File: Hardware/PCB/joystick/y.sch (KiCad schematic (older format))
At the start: 19 parts, among them J6 AudioJack2, J7 AudioJack2, U2 TL074

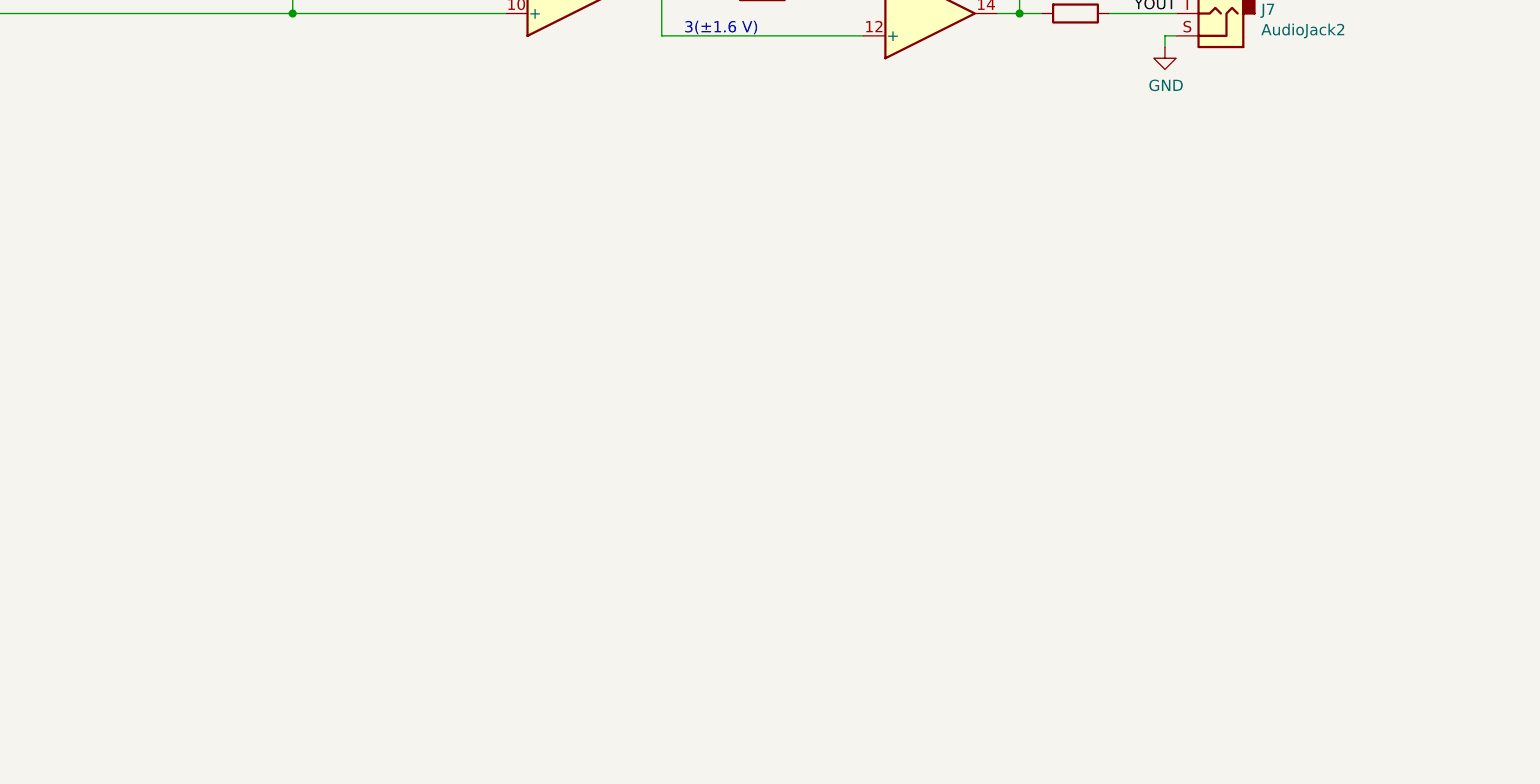
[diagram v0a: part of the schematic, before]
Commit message: Belated .gitignore; switch to panel mounted pots implying board and panel changes
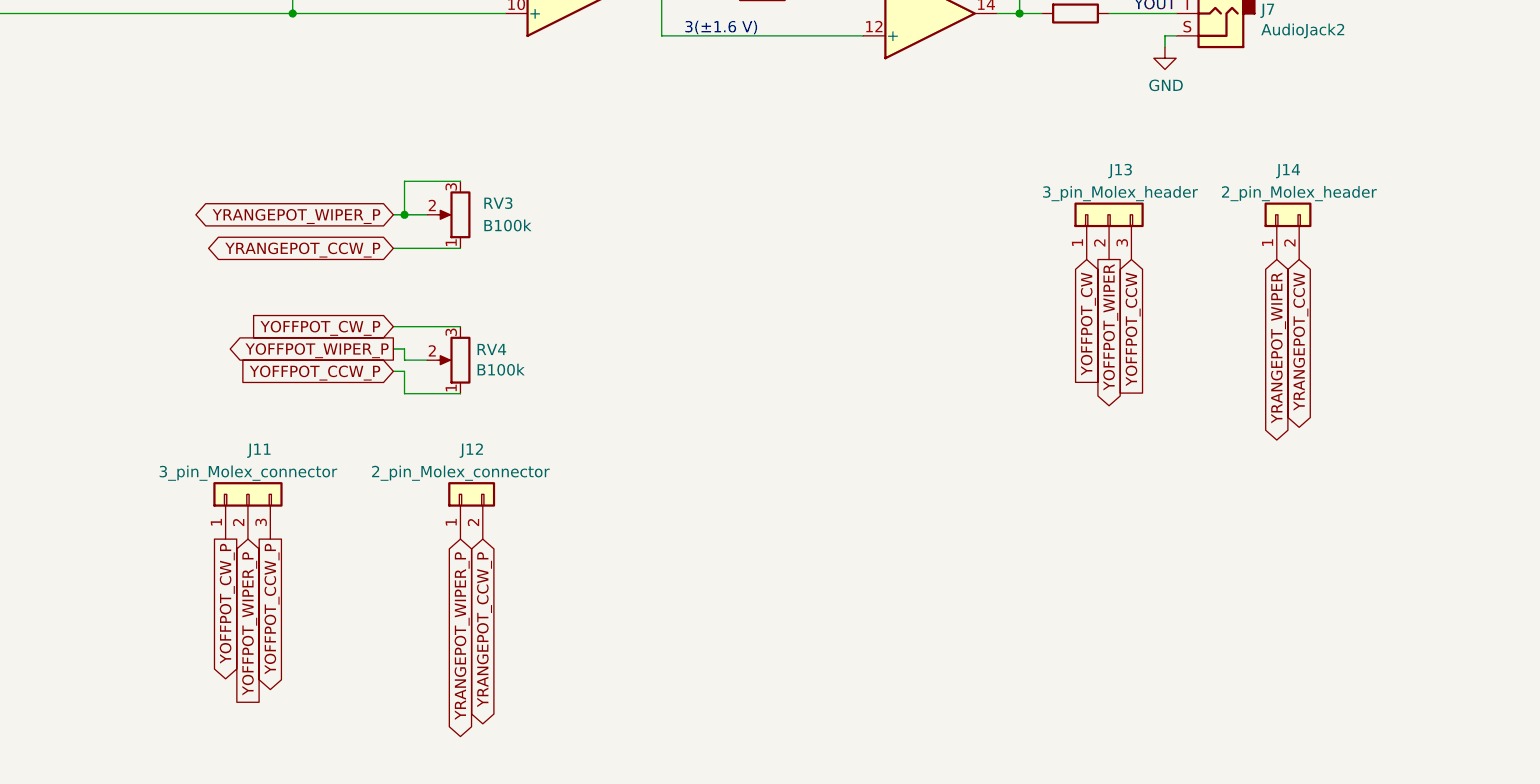
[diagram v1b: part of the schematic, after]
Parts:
- added J11: 3_pin_Molex_connector, symbol ao_symbols:3_pin_Molex_connector
- added J12: 2_pin_Molex_connector, symbol ao_symbols:2_pin_Molex_connector
- added J13: 3_pin_Molex_header, ao_tht:Molex_KK-254_AE-6410-03A_1x03_P2.54mm_Vertical, symbol ao_symbols:3_pin_Molex_header
- added J14: 2_pin_Molex_header, ao_tht:Molex_KK-254_AE-6410-02A_1x02_P2.54mm_Vertical, symbol ao_symbols:2_pin_Molex_header
- added RV3, RV4: B100k, ao_tht:Potentiometer_Alpha_16mm_Single_Vertical, symbol Device:R_POT
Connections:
- net YOFFPOT_CCW: now also J13.3 (Pin_3)
- net YOFFPOT_CW: now also J13.1 (Pin_1)
- net YOFFPOT_WIPER: now also J13.2 (Pin_2)
- net YRANGEPOT_CCW: now also J14.2 (Pin_2)
- net YRANGEPOT_WIPER: now also J14.1 (Pin_1)
- new net YOFFPOT_CCW_P: J11.3 (Pin_3), RV4.1
- new net YOFFPOT_CW_P: J11.1 (Pin_1), RV4.3
- new net YOFFPOT_WIPER_P: J11.2 (Pin_2), RV4.2
- new net YRANGEPOT_CCW_P: J12.2 (Pin_2), RV3.1
- new net YRANGEPOT_WIPER_P: J12.1 (Pin_1), RV3.2, RV3.3
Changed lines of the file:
@@
 $Descr A4 11693 8268
 encoding utf-8
-Sheet 2 3
+Sheet 2 2
 Title ""
 Date ""
@@
 Text GLabel 1850 2250 0    50   Output ~ 0
 YPOT_CCW
+Text GLabel 8600 4550 3    50   Input ~ 0
+YOFFPOT_CW
+Text GLabel 8700 4550 3    50   Output ~ 0
+YOFFPOT_WIPER
+Text GLabel 8800 4550 3    50   Input ~ 0
+YOFFPOT_CCW
+Text GLabel 9550 4550 3    50   BiDi ~ 0
+YRANGEPOT_CCW
+Text GLabel 9450 4550 3    50   BiDi ~ 0
+YRANGEPOT_WIPER
+$Comp
+L ao_symbols:3_pin_Molex_header J?
+U 1 1 617BD456
+P 8700 4350
+AR Path="/617BD456" Ref="J?"  Part="1"
+AR Path="/6157E61D/617BD456" Ref="J13"  Part="1"
+F 0 "J13" V 8900 4350 50  0000 R CNN
+F 1 "3_pin_Molex_header" V 8800 4650 50  0000 R CNN
+F 2 "ao_tht:Molex_KK-254_AE-6410-03A_1x03_P2.54mm_Vertical" H 8700 4350 50  0001 C CNN
+F 3 "" H 8700 4350 50  0001 C CNN
+F 4 "Tayda" H 8700 4350 50  0001 C CNN "Vendor"
+F 5 "A-805" H 8700 4350 50  0001 C CNN "SKU"
+	1    8700 4350
+	0    -1   -1   0
+$EndComp
+$Comp
+L ao_symbols:2_pin_Molex_header J?
+U 1 1 617BD45E
+P 9450 4350
+AR Path="/617BD45E" Ref="J?"  Part="1"
+AR Path="/6157E61D/617BD45E" Ref="J14"  Part="1"
+F 0 "J14" V 9650 4350 50  0000 R CNN
+F 1 "2_pin_Molex_header" V 9550 4600 50  0000 R CNN
+F 2 "ao_tht:Molex_KK-254_AE-6410-02A_1x02_P2.54mm_Vertical" H 9450 4350 50  0001 C CNN
+F 3 "" H 9450 4350 50  0001 C CNN
+F 4 "Tayda" H 9450 4350 50  0001 C CNN "Vendor"
+F 5 "A-804" H 9450 4350 50  0001 C CNN "SKU"
+	1    9450 4350
+	0    -1   -1   0
+$EndComp
+Wire Wire Line
+	5500 5050 5550 5050
+Wire Wire Line
+	5550 5050 5550 5150
+Wire Wire Line
+	5550 5150 5800 5150
+Wire Wire Line
+	5500 4850 5800 4850
+Wire Wire Line
+	5650 5000 5550 5000
+Wire Wire Line
+	5550 5000 5550 4950
+Wire Wire Line
+	5550 4950 5500 4950
+Wire Wire Line
+	5550 4350 5550 4200
+Wire Wire Line
+	5500 4350 5550 4350
+Connection ~ 5550 4350
+Text GLabel 5500 4350 0    50   BiDi ~ 0
+YRANGEPOT_WIPER_P
+Text GLabel 5500 4500 0    50   BiDi ~ 0
+YRANGEPOT_CCW_P
+Text GLabel 5500 4850 0    50   Input ~ 0
+YOFFPOT_CW_P
+Text GLabel 5500 4950 0    50   Output ~ 0
+YOFFPOT_WIPER_P
+Text GLabel 5500 5050 0    50   Input ~ 0
+YOFFPOT_CCW_P
+Wire Wire Line
+	5550 4200 5800 4200
+Wire Wire Line
+	5550 4350 5650 4350
+Wire Wire Line
+	5500 4500 5800 4500
+$Comp
+L Device:R_POT RV?
+U 1 1 617F3E12
+P 5800 4350
+AR Path="/617F3E12" Ref="RV?"  Part="1"
+AR Path="/61647DC3/617F3E12" Ref="RV?"  Part="1"
+AR Path="/6157E61D/617F3E12" Ref="RV3"  Part="1"
+F 0 "RV3" H 5700 4300 50  0000 R CNN
+F 1 "B100k" H 5700 4400 50  0000 R CNN
+F 2 "ao_tht:Potentiometer_Alpha_16mm_Single_Vertical" H 5800 4350 50  0001 C CNN
+F 3 "~" H 5800 4350 50  0001 C CNN
+	1    5800 4350
+	-1   0    0    1
+$EndComp
+Text GLabel 4750 5800 3    50   Output ~ 0
+YOFFPOT_CW_P
+Text GLabel 4850 5800 3    50   Input ~ 0
+YOFFPOT_WIPER_P
+Text GLabel 4950 5800 3    50   Output ~ 0
+YOFFPOT_CCW_P
+Text GLabel 5900 5800 3    50   BiDi ~ 0
+YRANGEPOT_CCW_P
+Text GLabel 5800 5800 3    50   BiDi ~ 0
+YRANGEPOT_WIPER_P
+$Comp
+L Device:R_POT RV?
+U 1 1 617F3E1D
+P 5800 5000
+AR Path="/617F3E1D" Ref="RV?"  Part="1"
+AR Path="/61647DC3/617F3E1D" Ref="RV?"  Part="1"
+AR Path="/6157E61D/617F3E1D" Ref="RV4"  Part="1"
+F 0 "RV4" H 5730 4954 50  0000 R CNN
+F 1 "B100k" H 5730 5045 50  0000 R CNN
+F 2 "ao_tht:Potentiometer_Alpha_16mm_Single_Vertical" H 5800 5000 50  0001 C CNN
+F 3 "~" H 5800 5000 50  0001 C CNN
+	1    5800 5000
+	-1   0    0    1
+$EndComp
+$Comp
+L ao_symbols:3_pin_Molex_connector J?
+U 1 1 617F3E25
+P 4850 5600
+AR Path="/617F3E25" Ref="J?"  Part="1"
+AR Path="/6157E61D/617F3E25" Ref="J11"  Part="1"
+F 0 "J11" V 5050 5600 50  0000 R CNN
+F 1 "3_pin_Molex_connector" V 4950 6000 50  0000 R CNN
+F 2 "" H 4850 5600 50  0001 C CNN
+F 3 "" H 4850 5600 50  0001 C CNN
+F 4 "Tayda" H 4850 5600 50  0001 C CNN "Vendor"
+F 5 "A-827" H 4850 5600 50  0001 C CNN "SKU"
+	1    4850 5600
+	0    -1   -1   0
+$EndComp
+$Comp
+L ao_symbols:2_pin_Molex_connector J?
+U 1 1 617F3E2D
+P 5800 5600
+AR Path="/617F3E2D" Ref="J?"  Part="1"
+AR Path="/6157E61D/617F3E2D" Ref="J12"  Part="1"
+F 0 "J12" V 6000 5600 50  0000 R CNN
+F 1 "2_pin_Molex_connector" V 5900 6000 50  0000 R CNN
+F 2 "" H 5800 5600 50  0001 C CNN
+F 3 "" H 5800 5600 50  0001 C CNN
+F 4 "Tayda" H 5800 5600 50  0001 C CNN "Vendor"
+F 5 "A-826" H 5800 5600 50  0001 C CNN "SKU"
+	1    5800 5600
+	0    -1   -1   0
+$EndComp
 $EndSCHEMATC
